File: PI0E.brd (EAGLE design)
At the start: 87 x 30 mm, 35 parts, among them T1 WE-LAN-10/100-BASE-T,74901001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

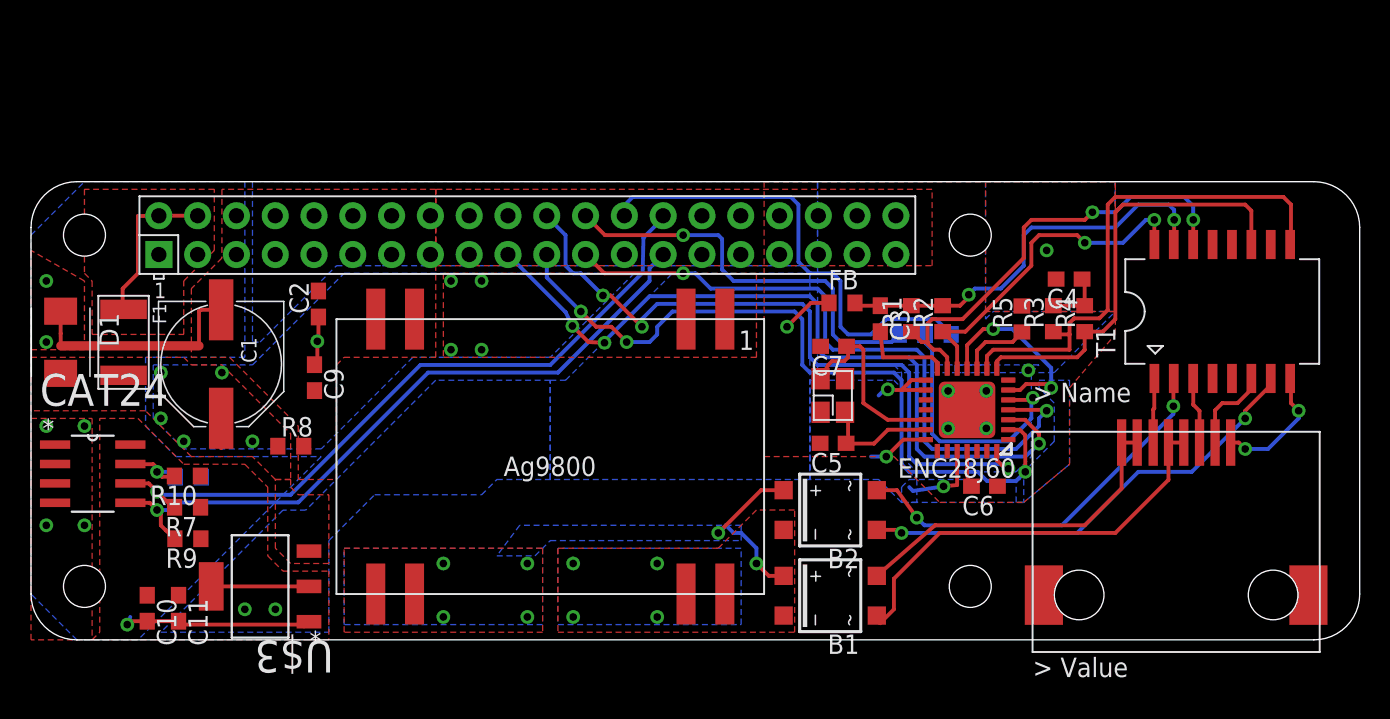
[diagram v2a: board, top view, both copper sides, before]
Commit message: Fixed silkscreen layer
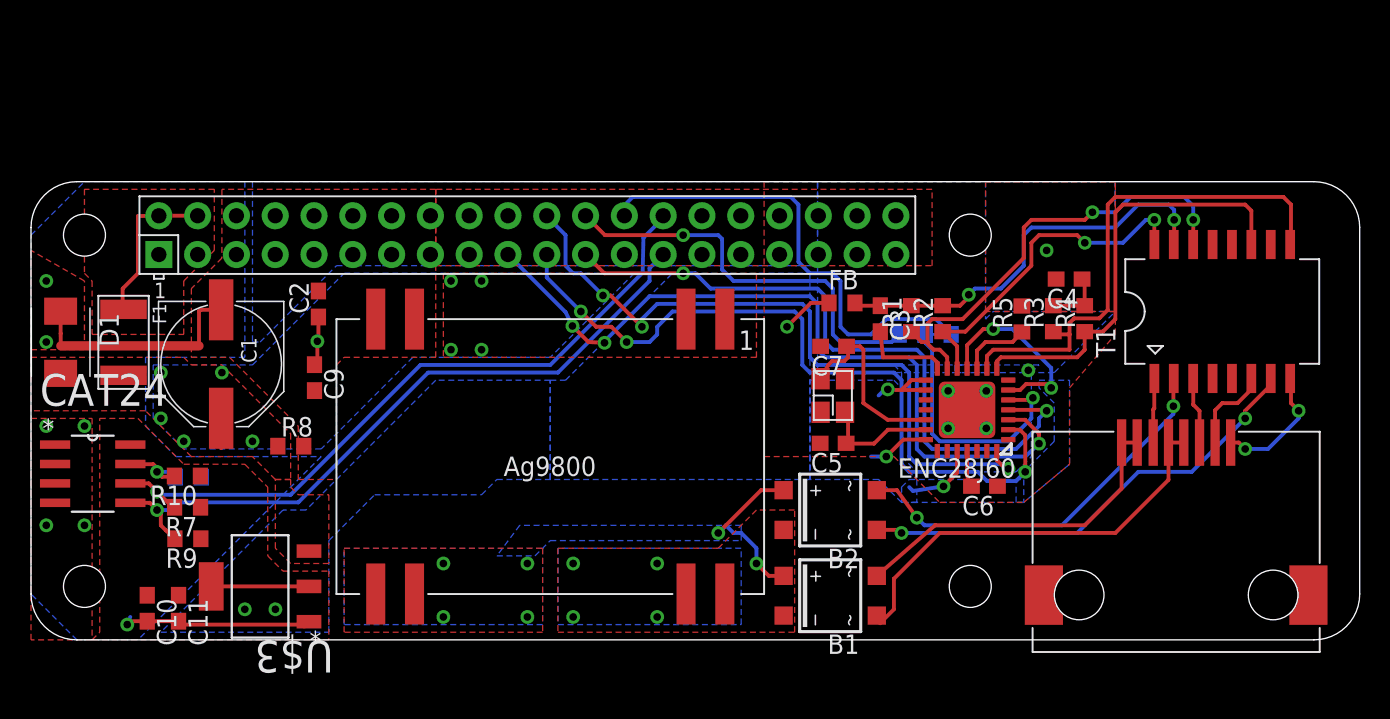
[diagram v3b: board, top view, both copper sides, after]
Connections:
- removed net !CE1: R11.2, U$1.26
- net !CEE: now also R11.2, U$1.26
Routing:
- net !CEE: track 17.1 -> 49.6 mm
- net !CE1: track 30.8 -> 0.00 mm
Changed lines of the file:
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@@
 <grid distance="19.6850394" unitdist="mil" unit="mil" style="lines" multiple="1" display="yes" altdistance="1.96850394" altunitdist="mil" altunit="mil"/>
 <layers>
-<layer number="1" name="Top" color="4" fill="1" visible="no" active="yes"/>
+<layer number="1" name="Top" color="4" fill="1" visible="yes" active="yes"/>
 <layer number="16" name="Bottom" color="1" fill="1" visible="yes" active="yes"/>
 <layer number="17" name="Pads" color="2" fill="1" visible="yes" active="yes"/>
@@
 <layer number="19" name="Unrouted" color="6" fill="1" visible="yes" active="yes"/>
 <layer number="20" name="Dimension" color="15" fill="1" visible="yes" active="yes"/>
-<layer number="21" name="tPlace" color="7" fill="1" visible="no" active="yes"/>
+<layer number="21" name="tPlace" color="7" fill="1" visible="yes" active="yes"/>
 <layer number="22" name="bPlace" color="7" fill="1" visible="no" active="yes"/>
 <layer number="23" name="tOrigins" color="15" fill="1" visible="yes" active="yes"/>
@@
 <layer number="46" name="Milling" color="3" fill="1" visible="no" active="yes"/>
 <layer number="47" name="Measures" color="7" fill="1" visible="no" active="yes"/>
-<layer number="48" name="Document" color="14" fill="1" visible="yes" active="yes"/>
+<layer number="48" name="Document" color="14" fill="1" visible="no" active="yes"/>
 <layer number="49" name="Reference" color="7" fill="1" visible="yes" active="yes"/>
 <layer number="50" name="dxf" color="7" fill="1" visible="no" active="no"/>
-<layer number="51" name="tDocu" color="14" fill="1" visible="yes" active="yes"/>
-<layer number="52" name="bDocu" color="24" fill="1" visible="yes" active="yes"/>
+<layer number="51" name="tDocu" color="14" fill="1" visible="no" active="yes"/>
+<layer number="52" name="bDocu" color="24" fill="1" visible="no" active="yes"/>
 <layer number="53" name="tGND_GNDA" color="7" fill="1" visible="no" active="no"/>
 <layer number="54" name="bGND_GNDA" color="7" fill="1" visible="no" active="no"/>
@@
 <vertex x="57" y="10"/>
 </polygon>
-<wire x1="60.64" y1="12.36" x2="60.64" y2="10.14" width="0.254" layer="1"/>
-<wire x1="60.64" y1="10.14" x2="59.75" y2="10.05" width="0.254" layer="1"/>
 <via x="59.75" y="10.05" extent="1-16" drill="0.5"/>
 <wire x1="59.75" y1="10.05" x2="57.75" y2="9.75" width="0.254" layer="16"/>
@@
 <wire x1="64.25" y1="20.35" x2="66.8" y2="17.8" width="0.254" layer="16"/>
 <wire x1="66.8" y1="17.8" x2="66.8" y2="16.5" width="0.254" layer="16"/>
+<wire x1="60.64" y1="12.36" x2="60.64" y2="10.94" width="0.254" layer="1"/>
+<wire x1="60.64" y1="10.94" x2="59.75" y2="10.05" width="0.254" layer="1"/>
 </signal>
 <signal name="N$18">
@@
 <wire x1="68" y1="20" x2="67.12" y2="20" width="0.254" layer="1"/>
 <wire x1="67.12" y1="20" x2="66.94" y2="20.18" width="0.254" layer="1"/>
-</signal>
-<signal name="!CE1">
-<contactref element="U$1" pad="26"/>
-<contactref element="R11" pad="2"/>
-<wire x1="60.25" y1="20" x2="59.25" y2="21" width="0.254" layer="16"/>
-<wire x1="59.25" y1="21" x2="56" y2="21" width="0.254" layer="16"/>
-<wire x1="56" y1="21" x2="55" y2="20" width="0.254" layer="16"/>
-<wire x1="55" y1="20" x2="53.5" y2="20" width="0.254" layer="16"/>
-<wire x1="53.5" y1="20" x2="53" y2="20.5" width="0.254" layer="16"/>
-<wire x1="53" y1="20.5" x2="53" y2="23.5" width="0.254" layer="16"/>
-<wire x1="53" y1="23.5" x2="52.5" y2="24" width="0.254" layer="16"/>
-<wire x1="52.5" y1="24" x2="51" y2="24" width="0.254" layer="16"/>
-<wire x1="51" y1="24" x2="50.25" y2="24.75" width="0.254" layer="16"/>
-<wire x1="50.25" y1="24.75" x2="50.25" y2="28.5" width="0.254" layer="16"/>
-<wire x1="50.25" y1="28.5" x2="49.75" y2="29" width="0.254" layer="16"/>
-<wire x1="49.75" y1="29" x2="39.4" y2="29" width="0.254" layer="16"/>
-<wire x1="39.4" y1="29" x2="38.85" y2="28.45" width="0.254" layer="16"/>
-<wire x1="38.85" y1="28.45" x2="38.85" y2="27.77" width="0.254" layer="16"/>
 </signal>
 <signal name="ID_SD">
@@
 <wire x1="65.6" y1="15.85" x2="65.5" y2="15.75" width="0.254" layer="16"/>
 <wire x1="65.5" y1="15.75" x2="65.5" y2="14.5" width="0.254" layer="16"/>
+<contactref element="R11" pad="2"/>
+<contactref element="U$1" pad="26"/>
+<wire x1="59.25" y1="21" x2="56" y2="21" width="0.254" layer="16"/>
+<wire x1="56" y1="21" x2="55" y2="20" width="0.254" layer="16"/>
+<wire x1="55" y1="20" x2="53.5" y2="20" width="0.254" layer="16"/>
+<wire x1="53.5" y1="20" x2="53" y2="20.5" width="0.254" layer="16"/>
+<wire x1="53" y1="20.5" x2="53" y2="23.5" width="0.254" layer="16"/>
+<wire x1="53" y1="23.5" x2="52.5" y2="24" width="0.254" layer="16"/>
+<wire x1="52.5" y1="24" x2="51" y2="24" width="0.254" layer="16"/>
+<wire x1="51" y1="24" x2="50.25" y2="24.75" width="0.254" layer="16"/>
+<wire x1="50.25" y1="24.75" x2="50.25" y2="28.5" width="0.254" layer="16"/>
+<wire x1="50.25" y1="28.5" x2="49.75" y2="29" width="0.254" layer="16"/>
+<wire x1="49.75" y1="29" x2="39.4" y2="29" width="0.254" layer="16"/>
+<wire x1="39.4" y1="29" x2="38.85" y2="28.45" width="0.254" layer="16"/>
+<wire x1="38.85" y1="28.45" x2="38.85" y2="27.77" width="0.254" layer="16"/>
+<wire x1="59.25" y1="21" x2="60.25" y2="20" width="0.254" layer="16"/>
+<wire x1="58.55" y1="20" x2="60.25" y2="20" width="0.1778" layer="16"/>
 </signal>
 <signal name="RD-">

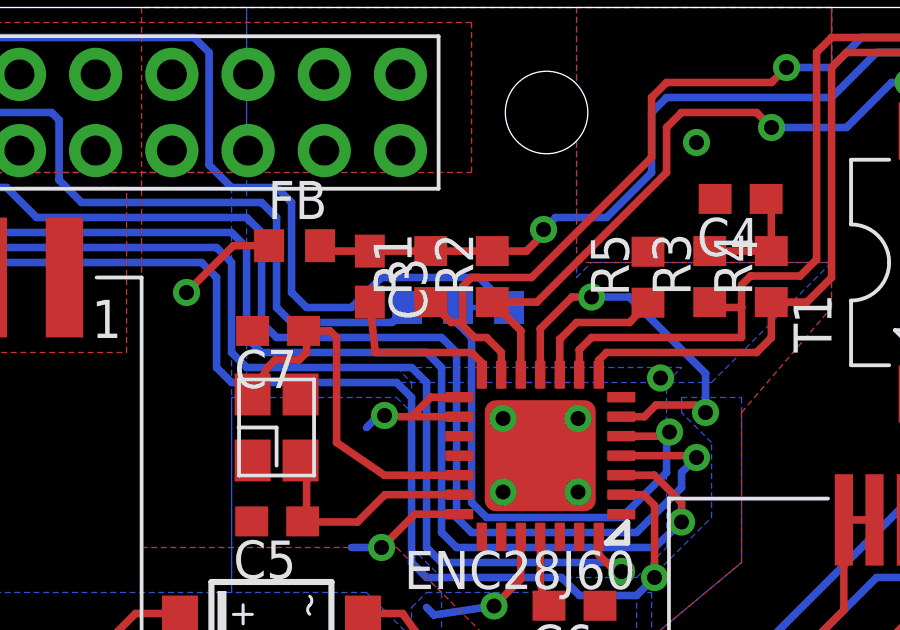
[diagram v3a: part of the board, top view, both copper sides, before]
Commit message: Changed default CE trace to CE0
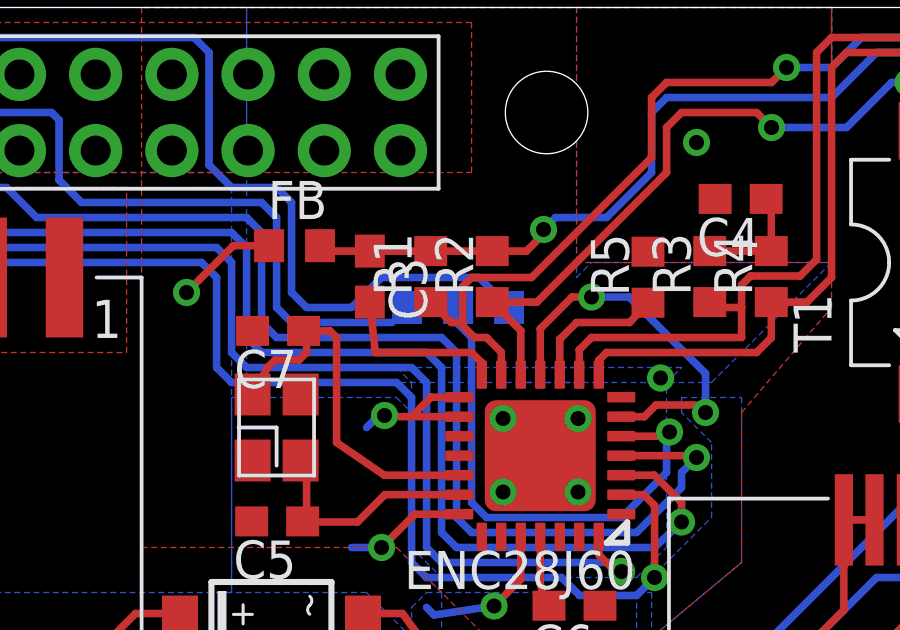
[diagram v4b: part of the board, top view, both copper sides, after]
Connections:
- new net !CE1: R11.2, U$1.26
- net !CE0: no longer R6.1
- net !CEE: now also R6.1; no longer R11.2, U$1.26
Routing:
- net !CE1: track 0.00 -> 30.8 mm
- net !CEE: track 49.6 -> 18.8 mm
- net !CE0: track 27.1 -> 26.4 mm
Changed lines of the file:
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@@
 <grid distance="19.6850394" unitdist="mil" unit="mil" style="lines" multiple="1" display="yes" altdistance="1.96850394" altunitdist="mil" altunit="mil"/>
 <layers>
-<layer number="1" name="Top" color="4" fill="1" visible="yes" active="yes"/>
+<layer number="1" name="Top" color="4" fill="1" visible="no" active="yes"/>
 <layer number="16" name="Bottom" color="1" fill="1" visible="yes" active="yes"/>
 <layer number="17" name="Pads" color="2" fill="1" visible="yes" active="yes"/>
@@
 <signal name="!CE0">
 <contactref element="U$1" pad="24"/>
-<contactref element="R6" pad="1"/>
-<wire x1="56.85" y1="20" x2="56.35" y2="19.5" width="0.254" layer="16"/>
 <wire x1="56.35" y1="19.5" x2="53" y2="19.5" width="0.254" layer="16"/>
 <wire x1="53" y1="19.5" x2="52.5" y2="20" width="0.254" layer="16"/>
@@
 <wire x1="65.6" y1="15.85" x2="65.5" y2="15.75" width="0.254" layer="16"/>
 <wire x1="65.5" y1="15.75" x2="65.5" y2="14.5" width="0.254" layer="16"/>
-<contactref element="R11" pad="2"/>
-<contactref element="U$1" pad="26"/>
-<wire x1="59.25" y1="21" x2="56" y2="21" width="0.254" layer="16"/>
-<wire x1="56" y1="21" x2="55" y2="20" width="0.254" layer="16"/>
-<wire x1="55" y1="20" x2="53.5" y2="20" width="0.254" layer="16"/>
-<wire x1="53.5" y1="20" x2="53" y2="20.5" width="0.254" layer="16"/>
-<wire x1="53" y1="20.5" x2="53" y2="23.5" width="0.254" layer="16"/>
-<wire x1="53" y1="23.5" x2="52.5" y2="24" width="0.254" layer="16"/>
-<wire x1="52.5" y1="24" x2="51" y2="24" width="0.254" layer="16"/>
-<wire x1="51" y1="24" x2="50.25" y2="24.75" width="0.254" layer="16"/>
-<wire x1="50.25" y1="24.75" x2="50.25" y2="28.5" width="0.254" layer="16"/>
-<wire x1="50.25" y1="28.5" x2="49.75" y2="29" width="0.254" layer="16"/>
-<wire x1="49.75" y1="29" x2="39.4" y2="29" width="0.254" layer="16"/>
-<wire x1="39.4" y1="29" x2="38.85" y2="28.45" width="0.254" layer="16"/>
-<wire x1="38.85" y1="28.45" x2="38.85" y2="27.77" width="0.254" layer="16"/>
-<wire x1="59.25" y1="21" x2="60.25" y2="20" width="0.254" layer="16"/>
-<wire x1="58.55" y1="20" x2="60.25" y2="20" width="0.1778" layer="16"/>
+<contactref element="R6" pad="1"/>
+<wire x1="58.55" y1="20" x2="56.85" y2="20" width="0.254" layer="16"/>
 </signal>
 <signal name="RD-">
@@
 </polygon>
 </signal>
+<signal name="!CE1">
+<contactref element="R11" pad="2"/>
+<contactref element="U$1" pad="26"/>
+<wire x1="59.25" y1="21" x2="56" y2="21" width="0.254" layer="16"/>
+<wire x1="56" y1="21" x2="55" y2="20" width="0.254" layer="16"/>
+<wire x1="55" y1="20" x2="53.5" y2="20" width="0.254" layer="16"/>
+<wire x1="53.5" y1="20" x2="53" y2="20.5" width="0.254" layer="16"/>
+<wire x1="53" y1="20.5" x2="53" y2="23.5" width="0.254" layer="16"/>
+<wire x1="53" y1="23.5" x2="52.5" y2="24" width="0.254" layer="16"/>
+<wire x1="52.5" y1="24" x2="51" y2="24" width="0.254" layer="16"/>
+<wire x1="51" y1="24" x2="50.25" y2="24.75" width="0.254" layer="16"/>
+<wire x1="50.25" y1="24.75" x2="50.25" y2="28.5" width="0.254" layer="16"/>
+<wire x1="50.25" y1="28.5" x2="49.75" y2="29" width="0.254" layer="16"/>
+<wire x1="49.75" y1="29" x2="39.4" y2="29" width="0.254" layer="16"/>
+<wire x1="39.4" y1="29" x2="38.85" y2="28.45" width="0.254" layer="16"/>
+<wire x1="38.85" y1="28.45" x2="38.85" y2="27.77" width="0.254" layer="16"/>
+<wire x1="59.25" y1="21" x2="60.25" y2="20" width="0.254" layer="16"/>
+</signal>
 </signals>

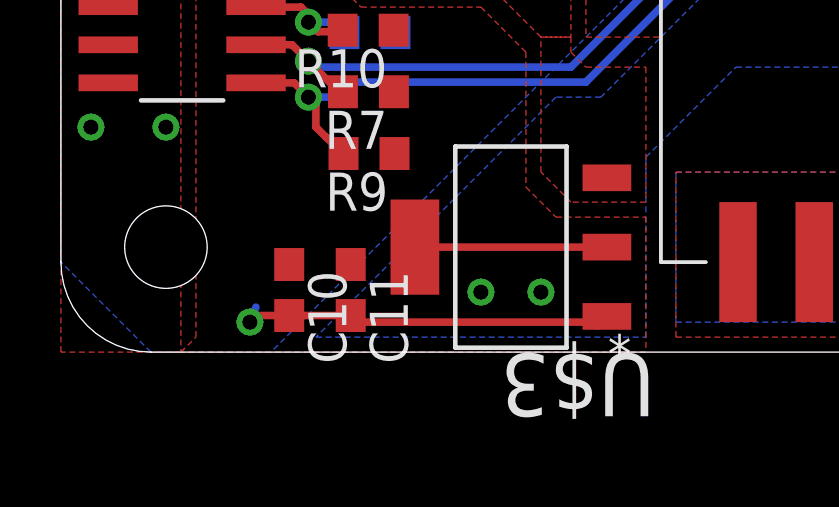
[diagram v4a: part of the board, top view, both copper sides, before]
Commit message: Changed cap from 0603 to 0805
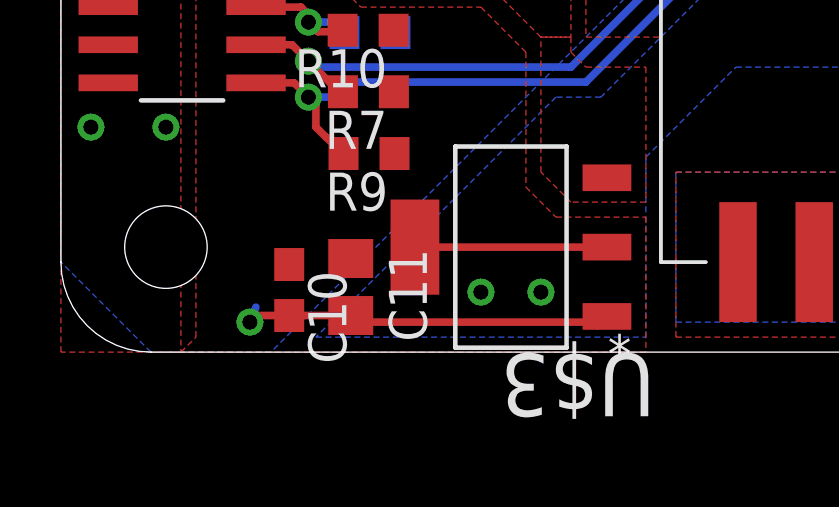
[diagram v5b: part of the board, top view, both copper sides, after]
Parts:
- C11: device rcl:C0603 -> rcl:C0805
- moved C11 0.10 mm to (9.66, 2.17)
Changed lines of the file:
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@@
 <grid distance="19.6850394" unitdist="mil" unit="mil" style="lines" multiple="1" display="yes" altdistance="1.96850394" altunitdist="mil" altunit="mil"/>
 <layers>
-<layer number="1" name="Top" color="4" fill="1" visible="no" active="yes"/>
+<layer number="1" name="Top" color="4" fill="1" visible="yes" active="yes"/>
 <layer number="16" name="Bottom" color="1" fill="1" visible="yes" active="yes"/>
 <layer number="17" name="Pads" color="2" fill="1" visible="yes" active="yes"/>
@@
 <element name="C1" library="rcl" package="PANASONIC_F" value="470uF" x="12.45" y="18.06" rot="R270"/>
 <element name="C10" library="rcl" package="C0603" value="100nF" x="7.61" y="2.07" rot="R270"/>
-<element name="C11" library="rcl" package="C0603" value="100uF" x="9.66" y="2.07" rot="R270"/>
+<element name="C11" library="rcl" package="C0805" value="100uF" x="9.66" y="2.17" rot="R270"/>
 <element name="C2" library="rcl" package="C0603" value=".1uF" x="18.82" y="21.99" rot="R90"/>
 <element name="C3" library="rcl" package="C0603" value=".1uF" x="55.61" y="21.03" rot="R270"/>
